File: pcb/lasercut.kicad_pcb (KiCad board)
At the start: 2 copper layers, 338.6 x 105.3 mm, 145 parts, among them SW1 SW_Push, SW10 SW_Push, SW11 SW_Push, SW12 SW_Push, SW13 SW_Push, SW14 SW_Push, SW15 SW_Push, SW16 SW_Push, SW17 SW_Push, SW18 SW_Push, SW19 SW_Push, SW2 SW_Push, SW20 SW_Push, SW21 SW_Push, SW22 SW_Push, SW23 SW_Push, SW24 SW_Push, SW25 SW_Push, SW26 SW_Push, SW27 SW_Push, SW28 SW_Push, SW29 SW_Push, SW3 SW_Push, SW30 SW_Push, SW31 SW_Push, SW32 SW_Push, SW33 SW_Push, SW34 SW_Push, SW35 SW_Push, SW36 SW_Push, SW37 SW_Push, SW38 SW_Push, SW39 SW_Push, SW4 SW_Push, SW40 SW_Push, SW41 SW_Push, SW42 SW_Push, SW43 SW_Push, SW44 SW_Push, SW45 SW_Push, SW46 SW_Push, SW47 SW_Push, SW48 SW_Push, SW49 SW_Push, SW5 SW_Push, SW50 SW_Push, SW51 SW_Push, SW52 SW_Push, SW53 SW_Push, SW54 SW_Push, SW55 SW_Push, SW56 SW_Push, SW57 SW_Push, SW58 SW_Push, SW59 SW_Push, SW6 SW_Push, SW60 SW_Push, SW61 SW_Push, SW62 SW_Push, SW63 SW_Push, SW64 SW_Push, SW65 SW_Push, SW66 SW_Push, SW67 SW_Push, SW68 SW_Push, SW69 SW_Push, SW7 SW_Push, SW70 SW_Push, SW71 SW_Push, SW72 SW_Push, SW8 SW_Push, SW9 SW_Push, U1 Elite-C

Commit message: add gerber and more images
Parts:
- added M2: MountingHole_2.2mm_M2, MountingHole:MountingHole_2.2mm_M2, F.Cu at (22.4, 72.6)
- added M2: MountingHole_2.2mm_M2, MountingHole:MountingHole_2.2mm_M2, F.Cu at (272.6, 122.8)
- added M2: MountingHole_2.2mm_M2, MountingHole:MountingHole_2.2mm_M2, F.Cu at (272.6, 22.5)
- added M2: MountingHole_2.2mm_M2, MountingHole:MountingHole_2.2mm_M2, F.Cu at (356.0, 22.5)
- added M2: MountingHole_2.2mm_M2, MountingHole:MountingHole_2.2mm_M2, F.Cu at (105.8, 122.8)
- added M2: MountingHole_2.2mm_M2, MountingHole:MountingHole_2.2mm_M2, F.Cu at (356.0, 72.6)
- added M2: MountingHole_2.2mm_M2, MountingHole:MountingHole_2.2mm_M2, F.Cu at (356.0, 122.8)
- added M2: MountingHole_2.2mm_M2, MountingHole:MountingHole_2.2mm_M2, F.Cu at (189.2, 122.8)
- added M2: MountingHole_2.2mm_M2, MountingHole:MountingHole_2.2mm_M2, F.Cu at (22.4, 122.8)
- added M2: MountingHole_2.2mm_M2, MountingHole:MountingHole_2.2mm_M2, F.Cu at (22.4, 22.5)
- added M2: MountingHole_2.2mm_M2, MountingHole:MountingHole_2.2mm_M2, F.Cu at (105.8, 22.5)
- added M2: MountingHole_2.2mm_M2, MountingHole:MountingHole_2.2mm_M2, F.Cu at (189.2, 22.5)
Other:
- outline, holes or cut-outs redrawn
- board text added: "Lasercut v1.0 by lad1337"

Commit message: add batter headers
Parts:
- added J1: Conn_01x02_Male, Connector_PinHeader_2.54mm:PinHeader_1x02_P2.54mm_Horizontal, B.Cu at (307.6, 35.6)
- renumbered M2 to M1, M2 to M10, M2 to M11, M2 to M12, M2 to M3, M2 to M4, M2 to M5, M2 to M6, M2 to M7, M2 to M8, M2 to M9
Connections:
- U1 pad 24: unconnected-(U1-Pad24) -> BAT
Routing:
- net BAT: track 0.00 -> 89.5 mm
- net GND: track 18.8 -> 91.6 mm
- net row7: track 508.2 -> 521.9 mm
- net row6: track 489.0 -> 494.1 mm
- net row2: track 465.8 -> 469.3 mm
- net col5: track 363.8 -> 366.2 mm
- net row0: track 540.3 -> 542.6 mm
- net Net-(D32-Pad1): track 13.8 -> 16.1 mm
- net Net-(D16-Pad1): track 13.8 -> 16.1 mm
- net Net-(D57-Pad1): track 13.8 -> 16.1 mm
- net Net-(D53-Pad1): track 13.8 -> 16.1 mm
- net Net-(D55-Pad1): track 13.8 -> 16.1 mm
- net Net-(D49-Pad1): track 13.8 -> 16.1 mm
- net Net-(D54-Pad1): track 13.8 -> 16.1 mm
- net Net-(D70-Pad1): track 13.8 -> 16.1 mm
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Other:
- board text added: "+"
- board text added: "-"

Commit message: new freerouting version
need to redo the matrix/switch position
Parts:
- moved J1 61.6 mm to (342.9, 86.0)
- moved D30 1.00 mm to (303.9, 68.1)
- moved D33 1.00 mm to (46.7, 77.7)
- moved D46 1.00 mm to (42.0, 96.7)
- moved D58 1.00 mm to (280.1, 96.7)
- moved D61 1.00 mm to (42.0, 115.8)
- moved D62 1.00 mm to (65.8, 115.8)
- moved D63 1.00 mm to (89.6, 115.8)
- moved D64 1.00 mm to (122.9, 115.8)
- moved D66 1.00 mm to (189.6, 115.8)
- moved D67 1.00 mm to (227.7, 115.8)
- moved D68 1.00 mm to (251.5, 115.8)
- moved D69 1.00 mm to (275.3, 115.8)
- moved D1 1.00 mm to (39.6, 39.6)
- moved D10 1.00 mm to (211.1, 39.6)
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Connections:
- D10 pad 2: col1 -> col0
- D12 pad 2: col1 -> col2
- D13 pad 2: col1 -> col3
- D14 pad 2: col1 -> col4
- D15 pad 2: col1 -> col5
- D16 pad 2: col1 -> col6
- D17 pad 2: col2 -> col7
- D18 pad 2: col2 -> col8
- D19 pad 2: col2 -> col0
- D2 pad 2: col0 -> col1
- D20 pad 2: col2 -> col1
- D22 pad 2: col2 -> col3
- D23 pad 2: col2 -> col4
- D24 pad 2: col2 -> col5
- D25 pad 2: col3 -> col6
- D26 pad 2: col3 -> col7
- D27 pad 2: col3 -> col8
- D28 pad 2: col3 -> col0
- D29 pad 2: col3 -> col1
- D3 pad 2: col0 -> col2
- D30 pad 2: col3 -> col2
- D32 pad 2: col3 -> col4
- D33 pad 2: col4 -> col5
- D34 pad 2: col4 -> col6
- D35 pad 2: col4 -> col7
- D36 pad 2: col4 -> col8
- D37 pad 2: col4 -> col0
- D38 pad 2: col4 -> col1
- D39 pad 2: col4 -> col2
- D4 pad 2: col0 -> col3
- D40 pad 2: col4 -> col3
- D41 pad 2: col5 -> col4
- D43 pad 2: col5 -> col6
- D44 pad 2: col5 -> col7
- D45 pad 2: col5 -> col8
- D46 pad 2: col5 -> col0
- D47 pad 2: col5 -> col1
- D48 pad 2: col5 -> col2
- D49 pad 2: col6 -> col3
- D5 pad 2: col0 -> col4
- D50 pad 2: col6 -> col4
- D51 pad 2: col6 -> col5
- D53 pad 2: col6 -> col7
- D54 pad 2: col6 -> col8
- D55 pad 2: col6 -> col0
- D56 pad 2: col6 -> col1
- D57 pad 2: col7 -> col2
- D58 pad 2: col7 -> col3
- D59 pad 2: col7 -> col4
- D6 pad 2: col0 -> col5
- D60 pad 2: col7 -> col5
- D61 pad 2: col7 -> col6
- D63 pad 2: col7 -> col8
- D64 pad 2: col7 -> col0
- D65 pad 2: col8 -> col1
- D66 pad 2: col8 -> col2
- D67 pad 2: col8 -> col3
- D68 pad 2: col8 -> col4
- D69 pad 2: col8 -> col5
- D7 pad 2: col0 -> col6
- D70 pad 2: col8 -> col6
- D71 pad 2: col8 -> col7
- D8 pad 2: col0 -> col7
- D9 pad 2: col1 -> col8
- SW1 pad 1: row0 -> Net-(SW1-Pad1)
- SW10 pad 1: row1 -> Net-(SW10-Pad1)
- SW11 pad 1: row2 -> Net-(SW10-Pad1)
- SW12 pad 1: row3 -> Net-(SW10-Pad1)
- SW13 pad 1: row4 -> Net-(SW10-Pad1)
- SW14 pad 1: row5 -> Net-(SW10-Pad1)
- SW15 pad 1: row6 -> Net-(SW10-Pad1)
- SW16 pad 1: row7 -> Net-(SW10-Pad1)
- SW17 pad 1: row0 -> Net-(SW10-Pad1)
- SW18 pad 1: row1 -> Net-(SW10-Pad1)
- SW19 pad 1: row2 -> Net-(SW19-Pad1)
- SW2 pad 1: row1 -> Net-(SW1-Pad1)
- SW20 pad 1: row3 -> Net-(SW19-Pad1)
- SW21 pad 1: row4 -> Net-(SW19-Pad1)
- SW22 pad 1: row5 -> Net-(SW19-Pad1)
- SW23 pad 1: row6 -> Net-(SW19-Pad1)
- SW24 pad 1: row7 -> Net-(SW19-Pad1)
- SW25 pad 1: row0 -> Net-(SW19-Pad1)
- SW26 pad 1: row1 -> Net-(SW19-Pad1)
- SW27 pad 1: row2 -> Net-(SW19-Pad1)
- SW28 pad 1: row3 -> Net-(SW28-Pad1)
- SW29 pad 1: row4 -> Net-(SW28-Pad1)
- SW3 pad 1: row2 -> Net-(SW1-Pad1)
- SW30 pad 1: row5 -> Net-(SW28-Pad1)
- SW31 pad 1: row6 -> Net-(SW28-Pad1)
- SW32 pad 1: row7 -> Net-(SW28-Pad1)
- SW33 pad 1: row0 -> Net-(SW28-Pad1)
- SW34 pad 1: row1 -> Net-(SW28-Pad1)
- SW35 pad 1: row2 -> Net-(SW28-Pad1)
- SW36 pad 1: row3 -> Net-(SW28-Pad1)
- SW37 pad 1: row4 -> Net-(SW37-Pad1)
- SW38 pad 1: row5 -> Net-(SW37-Pad1)
- SW39 pad 1: row6 -> Net-(SW37-Pad1)
- SW4 pad 1: row3 -> Net-(SW1-Pad1)
- SW40 pad 1: row7 -> Net-(SW37-Pad1)
- SW41 pad 1: row0 -> Net-(SW37-Pad1)
- SW42 pad 1: row1 -> Net-(SW37-Pad1)
- SW43 pad 1: row2 -> Net-(SW37-Pad1)
- SW44 pad 1: row3 -> Net-(SW37-Pad1)
- SW45 pad 1: row4 -> Net-(SW37-Pad1)
- SW46 pad 1: row5 -> Net-(SW46-Pad1)
- SW47 pad 1: row6 -> Net-(SW46-Pad1)
- SW48 pad 1: row7 -> Net-(SW46-Pad1)
- SW49 pad 1: row0 -> Net-(SW46-Pad1)
- SW5 pad 1: row4 -> Net-(SW1-Pad1)
- SW50 pad 1: row1 -> Net-(SW46-Pad1)
- SW51 pad 1: row2 -> Net-(SW46-Pad1)
- SW52 pad 1: row3 -> Net-(SW46-Pad1)
- SW53 pad 1: row4 -> Net-(SW46-Pad1)
- SW54 pad 1: row5 -> Net-(SW46-Pad1)
- SW55 pad 1: row6 -> Net-(SW55-Pad1)
- SW56 pad 1: row7 -> Net-(SW55-Pad1)
- SW57 pad 1: row0 -> Net-(SW55-Pad1)
- SW58 pad 1: row1 -> Net-(SW55-Pad1)
- SW59 pad 1: row2 -> Net-(SW55-Pad1)
- SW6 pad 1: row5 -> Net-(SW1-Pad1)
- SW60 pad 1: row3 -> Net-(SW55-Pad1)
- SW61 pad 1: row4 -> Net-(SW55-Pad1)
- SW62 pad 1: row5 -> Net-(SW55-Pad1)
- SW63 pad 1: row6 -> Net-(SW55-Pad1)
- SW64 pad 1: row7 -> Net-(SW64-Pad1)
- SW65 pad 1: row0 -> Net-(SW64-Pad1)
- SW66 pad 1: row1 -> Net-(SW64-Pad1)
- SW67 pad 1: row2 -> Net-(SW64-Pad1)
- SW68 pad 1: row3 -> Net-(SW64-Pad1)
- SW69 pad 1: row4 -> Net-(SW64-Pad1)
- SW7 pad 1: row6 -> Net-(SW1-Pad1)
- SW70 pad 1: row5 -> Net-(SW64-Pad1)
- SW71 pad 1: row6 -> Net-(SW64-Pad1)
- SW72 pad 1: row7 -> Net-(SW64-Pad1)
- SW8 pad 1: row7 -> Net-(SW1-Pad1)
- SW9 pad 1: row0 -> Net-(SW1-Pad1)
- U1 pad 16: col6 -> col5
- U1 pad 17: col5 -> col4
- U1 pad 18: col4 -> col3
- U1 pad 19: col3 -> col2
- U1 pad 20: col2 -> unconnected-(U1-Pad20)
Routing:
- net row5: track 552.5 -> 0.00 mm
- net row0: track 542.6 -> 0.00 mm
- net row1: track 534.4 -> 0.00 mm
- net row7: track 521.9 -> 0.00 mm, vias 1 -> 0
- net row4: track 504.4 -> 0.00 mm, vias 1 -> 0
- net row6: track 494.1 -> 0.00 mm, vias 1 -> 0
- net row2: track 469.3 -> 0.00 mm, vias 3 -> 0
- net row3: track 452.7 -> 0.00 mm
- net col5: track 366.2 -> 0.00 mm
- net col7: track 325.8 -> 0.00 mm
- net col2: track 303.8 -> 0.00 mm, vias 1 -> 0
- net col0: track 302.8 -> 0.00 mm
- net col4: track 288.0 -> 0.00 mm, vias 1 -> 0
- net col8: track 270.4 -> 0.00 mm
- net col6: track 236.4 -> 0.00 mm, vias 1 -> 0
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
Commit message: new pcb kicad project
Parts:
- removed J1: Conn_01x02_Male, Connector_PinHeader_2.54mm:PinHeader_1x02_P2.54mm_Horizontal
- removed M1, M10, M11, M12, M2, M3, M4, M5, M6, M7, M8, M9: MountingHole_2.2mm_M2, MountingHole:MountingHole_2.2mm_M2
- removed U1: Elite-C, Keebio-Parts:Elite-C
- added REF**1: MountingHole_2.2mm_M2, MountingHole:MountingHole_2.2mm_M2, F.Cu at (22.6, 22.4)
- added REF**10: MountingHole_2.2mm_M2, MountingHole:MountingHole_2.2mm_M2, F.Cu at (272.8, 122.7)
- added REF**11: MountingHole_2.2mm_M2, MountingHole:MountingHole_2.2mm_M2, F.Cu at (356.1, 122.7)
- added REF**2: MountingHole_2.2mm_M2, MountingHole:MountingHole_2.2mm_M2, F.Cu at (106.0, 22.4)
- added REF**3: MountingHole_2.2mm_M2, MountingHole:MountingHole_2.2mm_M2, F.Cu at (189.3, 22.4)
- added REF**4: MountingHole_2.2mm_M2, MountingHole:MountingHole_2.2mm_M2, F.Cu at (272.8, 22.4)
- added REF**5: MountingHole_2.2mm_M2, MountingHole:MountingHole_2.2mm_M2, F.Cu at (356.1, 22.4)
- added REF**6: MountingHole_2.2mm_M2, MountingHole:MountingHole_2.2mm_M2, F.Cu at (22.6, 72.6)
- added REF**7: MountingHole_2.2mm_M2, MountingHole:MountingHole_2.2mm_M2, F.Cu at (22.6, 122.7)
- added REF**8: MountingHole_2.2mm_M2, MountingHole:MountingHole_2.2mm_M2, F.Cu at (106.0, 122.7)
- added REF**9: MountingHole_2.2mm_M2, MountingHole:MountingHole_2.2mm_M2, F.Cu at (189.3, 122.7)
- added U: ProMicro, Keebio-Parts:ArduinoProMicro, F.Cu at (335.4, 72.6)
- D1, D10, D11, D12, D13, D14, D15, D16, D17, D18, D19, D2, D20, D21, D22, D23, D24, D25, D26, D27, D28, D29, D3, D31, D32, D33, D34, D35, D36, D37, D38, D39, D4, D40, D41, D42, D43, D44, D45, D46, D47, D48, D49, D5, D50, D51, D52, D53, D54, D55, D56, D57, D58, D59, D6, D60, D61, D62, D63, D64, D65, D66, D67, D68, D69, D7, D70, D71, D72, D8, D9: value D -> 1N4148WS; footprint Diode_SMD:D_SOD-128 -> Diode_SMD:D_SOD-323F
- D30: footprint Diode_SMD:D_SOD-128 -> Diode_SMD:D_SOD-323F
- SW1, SW10, SW11, SW12, SW13, SW15, SW16, SW18, SW19, SW2, SW20, SW21, SW22, SW23, SW24, SW25, SW26, SW27, SW28, SW29, SW3, SW31, SW32, SW34, SW35, SW36, SW37, SW38, SW39, SW4, SW40, SW41, SW42, SW43, SW44, SW45, SW47, SW48, SW49, SW5, SW50, SW51, SW52, SW53, SW54, SW55, SW56, SW57, SW59, SW6, SW60, SW65, SW7, SW70, SW71, SW72, SW8, SW9: footprint MX_Only:MXOnly-1U-Hotswap-Antishear -> Switch_Keyboard_Hotswap_Kailh:SW_Hotswap_Kailh_MX_plated_1.00u
- SW14: footprint MX_Only:MXOnly-1U-Hotswap-Antishear -> Switch_Keyboard_Hotswap_Kailh:SW_Hotswap_Kailh_MX_plated_2.00u
- SW17: footprint MX_Only:MXOnly-1U-Hotswap-Antishear -> Switch_Keyboard_Hotswap_Kailh:SW_Hotswap_Kailh_MX_plated_1.50u
- SW30: footprint MX_Only:MXOnly-1U-Hotswap-Antishear -> Switch_Keyboard_Hotswap_Kailh:SW_Hotswap_Kailh_MX_plated_ISOEnter
- SW33, SW58: footprint MX_Only:MXOnly-1U-Hotswap-Antishear -> Switch_Keyboard_Hotswap_Kailh:SW_Hotswap_Kailh_MX_plated_1.75u
- SW46, SW61, SW62, SW63, SW67, SW68, SW69: footprint MX_Only:MXOnly-1U-Hotswap-Antishear -> Switch_Keyboard_Hotswap_Kailh:SW_Hotswap_Kailh_MX_plated_1.25u
- SW64: footprint MX_Only:MXOnly-1U-Hotswap-Antishear -> Switch_Keyboard_Hotswap_Kailh:SW_Hotswap_Kailh_MX_plated_2.25u
- SW66: footprint MX_Only:MXOnly-1U-Hotswap-Antishear -> Switch_Keyboard_Hotswap_Kailh:SW_Hotswap_Kailh_MX_plated_2.75u
- turned D1 to 90 degrees
- turned D10 to 90 degrees
- turned D11 to 90 degrees
- turned D12 to 90 degrees
- turned D13 to 90 degrees
- turned D14 to 90 degrees
- turned D15 to 90 degrees
- turned D16 to 90 degrees
- turned D17 to 90 degrees
- turned D18 to 90 degrees
- turned D19 to 90 degrees
- turned D2 to 90 degrees
- turned D20 to 90 degrees
- turned D21 to 90 degrees
- turned D22 to 90 degrees
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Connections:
- D1 pad 1: Net-(D1-Pad1) -> ROW0
- D1 pad 2: col0 -> N$1
- D10 pad 1: Net-(D10-Pad1) -> ROW5
- D10 pad 2: col0 -> N$10
- D11 pad 1: Net-(D11-Pad1) -> ROW5
- D11 pad 2: col1 -> N$11
- D12 pad 1: Net-(D12-Pad1) -> ROW5
- D12 pad 2: col2 -> N$12
- D13 pad 1: Net-(D13-Pad1) -> ROW5
- D13 pad 2: col3 -> N$13
- D14 pad 1: Net-(D14-Pad1) -> ROW5
- D14 pad 2: col4 -> N$14
- D15 pad 1: Net-(D15-Pad1) -> ROW5
- D15 pad 2: col5 -> N$15
- D16 pad 1: Net-(D16-Pad1) -> ROW5
- D16 pad 2: col6 -> N$16
- D17 pad 1: Net-(D17-Pad1) -> ROW1
- D17 pad 2: col7 -> N$17
- D18 pad 1: Net-(D18-Pad1) -> ROW1
- D18 pad 2: col8 -> N$18
- D19 pad 1: Net-(D19-Pad1) -> ROW1
- D19 pad 2: col0 -> N$19
- D2 pad 1: Net-(D2-Pad1) -> ROW0
- D2 pad 2: col1 -> N$2
- D20 pad 1: Net-(D20-Pad1) -> ROW1
- D20 pad 2: col1 -> N$20
- D21 pad 1: Net-(D21-Pad1) -> ROW1
- D21 pad 2: col2 -> N$21
- D22 pad 1: Net-(D22-Pad1) -> ROW1
- D22 pad 2: col3 -> N$22
- D23 pad 1: Net-(D23-Pad1) -> ROW1
- D23 pad 2: col4 -> N$23
- D24 pad 1: Net-(D24-Pad1) -> ROW1
- D24 pad 2: col5 -> N$24
- D25 pad 1: Net-(D25-Pad1) -> ROW1
- D25 pad 2: col6 -> N$25
- D26 pad 1: Net-(D26-Pad1) -> ROW6
- D26 pad 2: col7 -> N$26
- D27 pad 1: Net-(D27-Pad1) -> ROW6
- D27 pad 2: col8 -> N$27
- D28 pad 1: Net-(D28-Pad1) -> ROW6
- D28 pad 2: col0 -> N$28
- D29 pad 1: Net-(D29-Pad1) -> ROW6
- D29 pad 2: col1 -> N$29
- D3 pad 1: Net-(D3-Pad1) -> ROW0
- D3 pad 2: col2 -> N$3
- D30 pad 1: Net-(D30-Pad1) -> ROW7
- D30 pad 2: col2 -> N$30
- D31 pad 1: Net-(D31-Pad1) -> ROW6
- D31 pad 2: col3 -> N$31
- D32 pad 1: Net-(D32-Pad1) -> ROW6
- D32 pad 2: col4 -> N$32
- D33 pad 1: Net-(D33-Pad1) -> ROW2
- D33 pad 2: col5 -> N$33
- D34 pad 1: Net-(D34-Pad1) -> ROW2
- D34 pad 2: col6 -> N$34
- D35 pad 1: Net-(D35-Pad1) -> ROW2
- D35 pad 2: col7 -> N$35
- D36 pad 1: Net-(D36-Pad1) -> ROW2
- D36 pad 2: col8 -> N$36
- D37 pad 1: Net-(D37-Pad1) -> ROW2
- D37 pad 2: col0 -> N$37
- D38 pad 1: Net-(D38-Pad1) -> ROW2
- D38 pad 2: col1 -> N$38
- D39 pad 1: Net-(D39-Pad1) -> ROW2
- D39 pad 2: col2 -> N$39
- D4 pad 1: Net-(D4-Pad1) -> ROW0
- D4 pad 2: col3 -> N$4
- D40 pad 1: Net-(D40-Pad1) -> ROW2
- D40 pad 2: col3 -> N$40
- D41 pad 1: Net-(D41-Pad1) -> ROW2
- D41 pad 2: col4 -> N$41
- D42 pad 1: Net-(D42-Pad1) -> ROW7
- D42 pad 2: col5 -> N$42
- D43 pad 1: Net-(D43-Pad1) -> ROW7
- D43 pad 2: col6 -> N$43
- D44 pad 1: Net-(D44-Pad1) -> ROW7
- D44 pad 2: col7 -> N$44
- D45 pad 1: Net-(D45-Pad1) -> ROW7
- D45 pad 2: col8 -> N$45
- D46 pad 1: Net-(D46-Pad1) -> ROW3
- D46 pad 2: col0 -> N$46
- D47 pad 1: Net-(D47-Pad1) -> ROW3
- D47 pad 2: col1 -> N$47
- D48 pad 1: Net-(D48-Pad1) -> ROW3
- D48 pad 2: col2 -> N$48
- D49 pad 1: Net-(D49-Pad1) -> ROW3
- D49 pad 2: col3 -> N$49
- D5 pad 1: Net-(D5-Pad1) -> ROW0
- D5 pad 2: col4 -> N$5
- D50 pad 1: Net-(D50-Pad1) -> ROW3
- D50 pad 2: col4 -> N$50
- D51 pad 1: Net-(D51-Pad1) -> ROW3
- D51 pad 2: col5 -> N$51
- D52 pad 1: Net-(D52-Pad1) -> ROW3
- D52 pad 2: col6 -> N$52
- D53 pad 1: Net-(D53-Pad1) -> ROW3
- D53 pad 2: col7 -> N$53
- D54 pad 1: Net-(D54-Pad1) -> ROW3
- D54 pad 2: col8 -> N$54
- D55 pad 1: Net-(D55-Pad1) -> ROW7
- D55 pad 2: col0 -> N$55
- D56 pad 1: Net-(D56-Pad1) -> ROW7
- D56 pad 2: col1 -> N$56
- D57 pad 1: Net-(D57-Pad1) -> ROW7
- D57 pad 2: col2 -> N$57
- D58 pad 1: Net-(D58-Pad1) -> ROW7
- D58 pad 2: col3 -> N$58
- D59 pad 1: Net-(D59-Pad1) -> ROW6
- D59 pad 2: col4 -> N$59
- D6 pad 1: Net-(D6-Pad1) -> ROW0
- D6 pad 2: col5 -> N$6
- D60 pad 1: Net-(D60-Pad1) -> ROW5
- D60 pad 2: col5 -> N$60
- D61 pad 1: Net-(D61-Pad1) -> ROW4
- D61 pad 2: col6 -> N$61
- D62 pad 1: Net-(D62-Pad1) -> ROW4
- D62 pad 2: col7 -> N$62
- D63 pad 1: Net-(D63-Pad1) -> ROW4
- D63 pad 2: col8 -> N$63
- D64 pad 1: Net-(D64-Pad1) -> ROW4
- D64 pad 2: col0 -> N$64
- D65 pad 1: Net-(D65-Pad1) -> ROW4
- D65 pad 2: col1 -> N$65
- D66 pad 1: Net-(D66-Pad1) -> ROW4
- D66 pad 2: col2 -> N$66
- D67 pad 1: Net-(D67-Pad1) -> ROW4
- D67 pad 2: col3 -> N$67
- D68 pad 1: Net-(D68-Pad1) -> ROW4
- D68 pad 2: col4 -> N$68
- D69 pad 1: Net-(D69-Pad1) -> ROW4
- D69 pad 2: col5 -> N$69
- D7 pad 1: Net-(D7-Pad1) -> ROW0
- D7 pad 2: col6 -> N$7
- D70 pad 1: Net-(D70-Pad1) -> ROW5
- D70 pad 2: col6 -> N$70
- D71 pad 1: Net-(D71-Pad1) -> ROW6
- D71 pad 2: col7 -> N$71
- D72 pad 1: Net-(D72-Pad1) -> ROW6
- D72 pad 2: col8 -> N$72
- D8 pad 1: Net-(D8-Pad1) -> ROW0
- D8 pad 2: col7 -> N$8
- D9 pad 1: Net-(D9-Pad1) -> ROW0
- D9 pad 2: col8 -> N$9
- SW1 pad 1: Net-(SW1-Pad1) -> COL0
- SW1 pad 2: Net-(D1-Pad1) -> N$1
- SW10 pad 1: Net-(SW10-Pad1) -> COL0
- SW10 pad 2: Net-(D10-Pad1) -> N$10
- SW11 pad 1: Net-(SW10-Pad1) -> COL1
- SW11 pad 2: Net-(D11-Pad1) -> N$11
- SW12 pad 1: Net-(SW10-Pad1) -> COL2
- SW12 pad 2: Net-(D12-Pad1) -> N$12
- SW13 pad 1: Net-(SW10-Pad1) -> COL3
- SW13 pad 2: Net-(D13-Pad1) -> N$13
- SW14 pad 1: Net-(SW10-Pad1) -> COL4
- SW14 pad 2: Net-(D14-Pad1) -> N$14
- SW15 pad 1: Net-(SW10-Pad1) -> COL5
- SW15 pad 2: Net-(D15-Pad1) -> N$15
- SW16 pad 1: Net-(SW10-Pad1) -> COL6
- SW16 pad 2: Net-(D16-Pad1) -> N$16
- SW17 pad 1: Net-(SW10-Pad1) -> COL0
- SW17 pad 2: Net-(D17-Pad1) -> N$17
- SW18 pad 1: Net-(SW10-Pad1) -> COL1
- SW18 pad 2: Net-(D18-Pad1) -> N$18
- SW19 pad 1: Net-(SW19-Pad1) -> COL2
- SW19 pad 2: Net-(D19-Pad1) -> N$19
- SW2 pad 1: Net-(SW1-Pad1) -> COL1
- SW2 pad 2: Net-(D2-Pad1) -> N$2
- SW20 pad 1: Net-(SW19-Pad1) -> COL3
- SW20 pad 2: Net-(D20-Pad1) -> N$20
- SW21 pad 1: Net-(SW19-Pad1) -> COL4
- SW21 pad 2: Net-(D21-Pad1) -> N$21
- SW22 pad 1: Net-(SW19-Pad1) -> COL5
- SW22 pad 2: Net-(D22-Pad1) -> N$22
- SW23 pad 1: Net-(SW19-Pad1) -> COL6
- SW23 pad 2: Net-(D23-Pad1) -> N$23
- SW24 pad 1: Net-(SW19-Pad1) -> COL7
- SW24 pad 2: Net-(D24-Pad1) -> N$24
- SW25 pad 1: Net-(SW19-Pad1) -> COL8
- SW25 pad 2: Net-(D25-Pad1) -> N$25
- SW26 pad 1: Net-(SW19-Pad1) -> COL0
- SW26 pad 2: Net-(D26-Pad1) -> N$26
- SW27 pad 1: Net-(SW19-Pad1) -> COL1
- SW27 pad 2: Net-(D27-Pad1) -> N$27
- SW28 pad 1: Net-(SW28-Pad1) -> COL2
- SW28 pad 2: Net-(D28-Pad1) -> N$28
- SW29 pad 1: Net-(SW28-Pad1) -> COL3
- SW29 pad 2: Net-(D29-Pad1) -> N$29
- SW3 pad 1: Net-(SW1-Pad1) -> COL2
- SW3 pad 2: Net-(D3-Pad1) -> N$3
- SW30 pad 1: Net-(SW28-Pad1) -> COL4
- SW30 pad 2: Net-(D30-Pad1) -> N$30
- SW31 pad 1: Net-(SW28-Pad1) -> COL5
- SW31 pad 2: Net-(D31-Pad1) -> N$31
- SW32 pad 1: Net-(SW28-Pad1) -> COL6
- SW32 pad 2: Net-(D32-Pad1) -> N$32
- SW33 pad 1: Net-(SW28-Pad1) -> COL0
- SW33 pad 2: Net-(D33-Pad1) -> N$33
- SW34 pad 1: Net-(SW28-Pad1) -> COL1
- SW34 pad 2: Net-(D34-Pad1) -> N$34
- SW35 pad 1: Net-(SW28-Pad1) -> COL2
- SW35 pad 2: Net-(D35-Pad1) -> N$35
- SW36 pad 1: Net-(SW28-Pad1) -> COL3
- SW36 pad 2: Net-(D36-Pad1) -> N$36
- SW37 pad 1: Net-(SW37-Pad1) -> COL4
- SW37 pad 2: Net-(D37-Pad1) -> N$37
- SW38 pad 1: Net-(SW37-Pad1) -> COL5
- SW38 pad 2: Net-(D38-Pad1) -> N$38
- SW39 pad 1: Net-(SW37-Pad1) -> COL6
- SW39 pad 2: Net-(D39-Pad1) -> N$39
- SW4 pad 1: Net-(SW1-Pad1) -> COL3
- SW4 pad 2: Net-(D4-Pad1) -> N$4
- SW40 pad 1: Net-(SW37-Pad1) -> COL7
- SW40 pad 2: Net-(D40-Pad1) -> N$40
- SW41 pad 1: Net-(SW37-Pad1) -> COL8
- SW41 pad 2: Net-(D41-Pad1) -> N$41
- SW42 pad 1: Net-(SW37-Pad1) -> COL0
- SW42 pad 2: Net-(D42-Pad1) -> N$42
- SW43 pad 1: Net-(SW37-Pad1) -> COL1
- SW43 pad 2: Net-(D43-Pad1) -> N$43
- SW44 pad 1: Net-(SW37-Pad1) -> COL2
- SW44 pad 2: Net-(D44-Pad1) -> N$44
- SW45 pad 1: Net-(SW37-Pad1) -> COL3
- SW45 pad 2: Net-(D45-Pad1) -> N$45
- SW46 pad 1: Net-(SW46-Pad1) -> COL0
- SW46 pad 2: Net-(D46-Pad1) -> N$46
- SW47 pad 1: Net-(SW46-Pad1) -> COL1
- SW47 pad 2: Net-(D47-Pad1) -> N$47
- SW48 pad 1: Net-(SW46-Pad1) -> COL2
- SW48 pad 2: Net-(D48-Pad1) -> N$48
- SW49 pad 1: Net-(SW46-Pad1) -> COL3
- SW49 pad 2: Net-(D49-Pad1) -> N$49
- SW5 pad 1: Net-(SW1-Pad1) -> COL4
- SW5 pad 2: Net-(D5-Pad1) -> N$5
- SW50 pad 1: Net-(SW46-Pad1) -> COL4
- SW50 pad 2: Net-(D50-Pad1) -> N$50
- SW51 pad 1: Net-(SW46-Pad1) -> COL5
- SW51 pad 2: Net-(D51-Pad1) -> N$51
- SW52 pad 1: Net-(SW46-Pad1) -> COL6
- SW52 pad 2: Net-(D52-Pad1) -> N$52
- SW53 pad 1: Net-(SW46-Pad1) -> COL7
- SW53 pad 2: Net-(D53-Pad1) -> N$53
- SW54 pad 1: Net-(SW46-Pad1) -> COL8
- SW54 pad 2: Net-(D54-Pad1) -> N$54
- SW55 pad 1: Net-(SW55-Pad1) -> COL5
- SW55 pad 2: Net-(D55-Pad1) -> N$55
- SW56 pad 1: Net-(SW55-Pad1) -> COL6
- SW56 pad 2: Net-(D56-Pad1) -> N$56
- SW57 pad 1: Net-(SW55-Pad1) -> COL7
- SW57 pad 2: Net-(D57-Pad1) -> N$57
- SW58 pad 1: Net-(SW55-Pad1) -> COL8
- SW58 pad 2: Net-(D58-Pad1) -> N$58
- SW59 pad 1: Net-(SW55-Pad1) -> COL4
- SW59 pad 2: Net-(D59-Pad1) -> N$59
- SW6 pad 1: Net-(SW1-Pad1) -> COL5
- SW6 pad 2: Net-(D6-Pad1) -> N$6
- SW60 pad 1: Net-(SW55-Pad1) -> COL8
- SW60 pad 2: Net-(D60-Pad1) -> N$60
- SW61 pad 1: Net-(SW55-Pad1) -> COL0
- SW61 pad 2: Net-(D61-Pad1) -> N$61
- SW62 pad 1: Net-(SW55-Pad1) -> COL1
- SW62 pad 2: Net-(D62-Pad1) -> N$62
- SW63 pad 1: Net-(SW55-Pad1) -> COL2
- SW63 pad 2: Net-(D63-Pad1) -> N$63
- SW64 pad 1: Net-(SW64-Pad1) -> COL3
- SW64 pad 2: Net-(D64-Pad1) -> N$64
- SW65 pad 1: Net-(SW64-Pad1) -> COL4
- SW65 pad 2: Net-(D65-Pad1) -> N$65
- SW66 pad 1: Net-(SW64-Pad1) -> COL5
- SW66 pad 2: Net-(D66-Pad1) -> N$66
- SW67 pad 1: Net-(SW64-Pad1) -> COL6
- SW67 pad 2: Net-(D67-Pad1) -> N$67
- SW68 pad 1: Net-(SW64-Pad1) -> COL7
- SW68 pad 2: Net-(D68-Pad1) -> N$68
- SW69 pad 1: Net-(SW64-Pad1) -> COL8
- SW69 pad 2: Net-(D69-Pad1) -> N$69
- SW7 pad 1: Net-(SW1-Pad1) -> COL6
- SW7 pad 2: Net-(D7-Pad1) -> N$7
- SW70 pad 1: Net-(SW64-Pad1) -> COL7
- SW70 pad 2: Net-(D70-Pad1) -> N$70
- SW71 pad 1: Net-(SW64-Pad1) -> COL8
- SW71 pad 2: Net-(D71-Pad1) -> N$71
- SW72 pad 1: Net-(SW64-Pad1) -> COL7
- SW72 pad 2: Net-(D72-Pad1) -> N$72
- SW8 pad 1: Net-(SW1-Pad1) -> COL7
- SW8 pad 2: Net-(D8-Pad1) -> N$8
- SW9 pad 1: Net-(SW1-Pad1) -> COL8
- SW9 pad 2: Net-(D9-Pad1) -> N$9
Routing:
- net COL4: track 0.00 -> 566.5 mm, vias 0 -> 1
- net COL6: track 0.00 -> 433.5 mm, vias 0 -> 1
- net COL5: track 0.00 -> 432.9 mm
- net COL0: track 0.00 -> 413.1 mm
- net COL1: track 0.00 -> 398.3 mm, vias 0 -> 1
- net COL2: track 0.00 -> 382.6 mm
- net COL3: track 0.00 -> 379.1 mm
- net ROW0: track 0.00 -> 335.5 mm, vias 0 -> 2
- net ROW3: track 0.00 -> 322.8 mm, vias 0 -> 1
- net COL7: track 0.00 -> 317.5 mm
- net ROW4: track 0.00 -> 314.1 mm, vias 0 -> 1
- net ROW1: track 0.00 -> 300.7 mm
- net ROW2: track 0.00 -> 290.5 mm
- net ROW5: track 0.00 -> 275.7 mm, vias 0 -> 1
- net COL8: track 0.00 -> 268.3 mm
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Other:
- board text removed: "+"
- board text removed: "-"
- board text removed: "Lasercut v1.0 by lad1337"

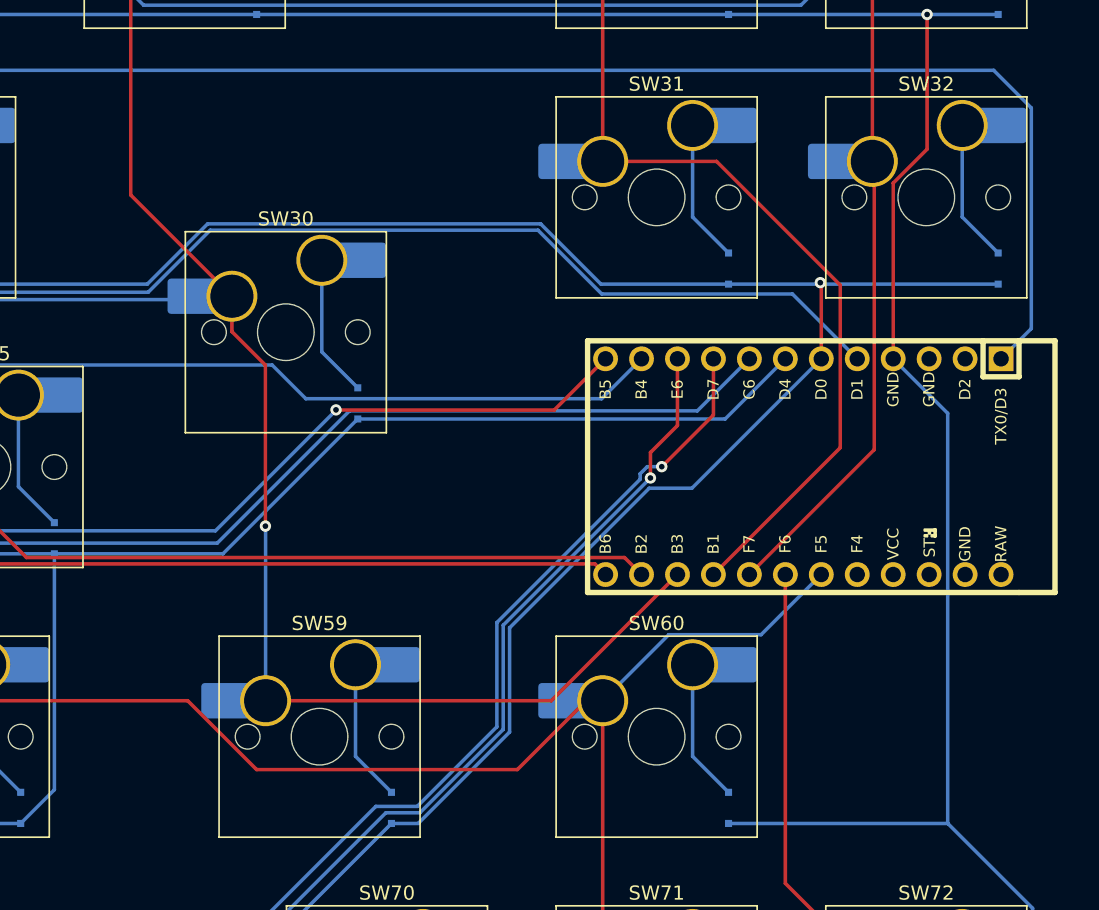
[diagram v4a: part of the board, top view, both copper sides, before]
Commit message: add battery connector and images
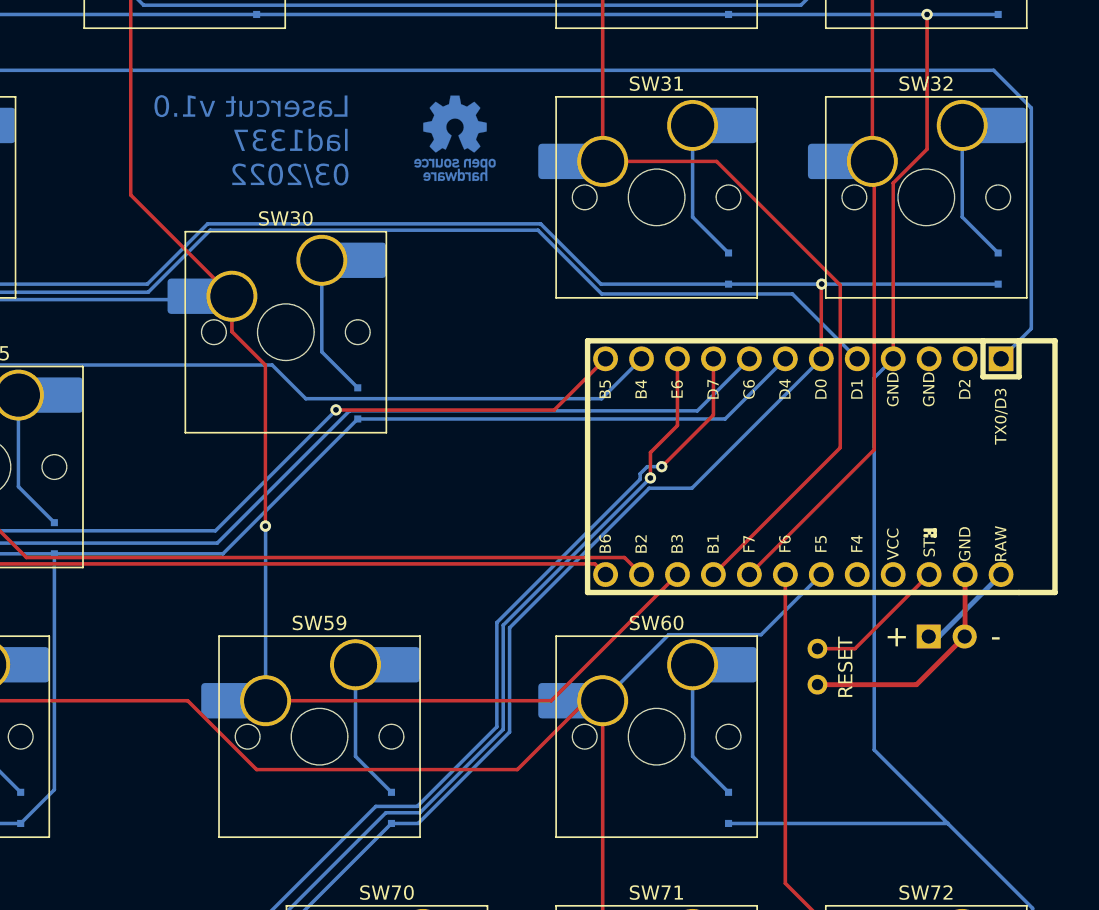
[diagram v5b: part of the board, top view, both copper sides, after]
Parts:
- added REF**: OSHW-Logo_5.7x6mm_Copper, Symbol:OSHW-Logo_5.7x6mm_Copper, B.Cu at (310.8, 49.4)
- added REF**: PinHeader_1x02_P2.54mm_Horizontal, Connector_PinHeader_2.54mm:PinHeader_1x02_P2.54mm_Horizontal, B.Cu at (344.3, 84.6)
- added RESET: TestPoint_2Pads_Pitch2.54mm_Drill0.8mm, TestPoint:TestPoint_2Pads_Pitch2.54mm_Drill0.8mm, B.Cu at (336.4, 88.0)
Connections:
- U pad 22: (no net) -> RST
- U pad 23: (no net) -> GND
- U pad 24: (no net) -> BAT
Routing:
- net GND: track 0.00 -> 16.2 mm
- net RST: track 0.00 -> 10.1 mm
- net BAT: track 0.00 -> 6.92 mm
- net ROW5: track 275.7 -> 276.8 mm
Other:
- board text added: "+"
- board text added: "-"
- board text added: "Lasercut v1.0 lad1337 03/2022"
- board text added: "RESET"
